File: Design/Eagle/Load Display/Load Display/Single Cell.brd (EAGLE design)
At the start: 68.2 x 83.8 mm, 12 parts

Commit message: Merge remote-tracking branch 'remotes/origin/Panic_Mode_Ben' into HEAD
Conflicts:
	Python/Master.py
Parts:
- removed 12VPOWER, I2C: M025MM, Ben-SF-Con:SCREWTERMINAL-5MM-2
- added JP2: (no value), Ben-SF-Con:2X3-SHROUDED
- added LED2: TLLR4400, led:LED3MM
- added R8: 1000, Ben-rcl:0207/15
- added U$2: (no value), Parts:DRIVER_BOARD_ADAFRUIT
- added U$4, U$5, U$6, U$7: SOLDER_JUMPER, Parts:SOLDER_JUMPER
- added U$8: (no value), Parts:DRIVER_BOARD
- DIS1: device Parts:4INTESTER -> Parts:7SEGMENT_BACKWARDS
- R1, R2, R3, R4, R5: device Ben-rcl:0207/10 -> Ben-rcl:0207/15
- U$1: value 5VREG -> SOLDER_JUMPER; device Parts:LM78XX -> Parts:SOLDER_JUMPER
- U$3: value HT16K33BRD -> SOLDER_JUMPER; device Parts:HT16K33BRKOUT -> Parts:SOLDER_JUMPER
- moved U$1 53.4 mm to (45.7, 26.7), flipped to the bottom, turned to 180 degrees
- moved R2 43.3 mm to (17.8, 69.9)
- moved R3 35.8 mm to (22.9, 11.4)
- moved R1 32.0 mm to (22.9, 69.9)
- moved R6 28.0 mm to (33.0, 69.9)
- moved R7 25.7 mm to (38.1, 69.9)
- moved U$3 24.1 mm to (45.7, 30.5), flipped to the bottom, turned to 180 degrees
- moved DIS1 21.6 mm to (17.8, 1.27)
- moved R4 20.7 mm to (31.7, 11.4)
- moved R5 8.52 mm to (38.1, 11.4)
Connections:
- removed net N$19: U$1.P$3, U$3.VDD
- removed net N$20: 12VPOWER.2, DIS1.8, U$1.P$1
- new net GND: JP2.2, JP2.6, LED2.K, U$1.P$1, U$2.G, U$2.GND, U$4.P$1, U$6.P$1, U$8.G, U$8.GND
- new net N$29: U$1.P$2, U$2.A0, U$3.P$1, U$8.A0
- new net SDA: JP2.3, U$2.SDA, U$8.SDA
- new net SSCL: JP2.4, U$2.SCL, U$8.SCL
- new net VCC12: DIS1.3, DIS1.8, JP2.1
- new net VCC5: JP2.5, R8.1, U$2.VCC, U$3.P$2, U$5.P$2, U$7.P$2, U$8.VCC
- net N$10: now also U$2.DRAIN2, U$8.DRAIN2; no longer U$3.C2
- net N$11: now also U$2.DRAIN3, U$8.DRAIN3; no longer U$3.C3
- net N$12: now also U$2.DRAIN4, U$8.DRAIN4; no longer U$3.C4
- net N$13: now also U$2.DRAIN5, U$8.DRAIN5; no longer U$3.C5
- net N$14: now also U$2.DRAIN6, U$8.DRAIN6; no longer U$3.C6
- net N$15: now also U$2.A1, U$4.P$2, U$5.P$1, U$8.A1; no longer I2C.1, U$3.SDA
- net N$16: now also U$2.A2, U$6.P$2, U$7.P$1, U$8.A2; no longer I2C.2, U$3.SCL
- net N$17: now also U$2.DRAIN7, U$8.DRAIN7; no longer 12VPOWER.1, U$1.P$2, U$3.GND
- net N$18: now also LED2.A, R8.2; no longer DIS1.5, U$3.C7
- net N$8: now also U$2.DRAIN0, U$8.DRAIN0; no longer U$3.C0
- net N$9: now also U$2.DRAIN1, U$8.DRAIN1; no longer U$3.C1
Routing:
- net GND: track 0.00 -> 172.5 mm
- net VCC12: track 0.00 -> 129.1 mm
- net VCC5: track 0.00 -> 93.9 mm
- net SSCL: track 0.00 -> 79.7 mm
- net N$10: track 99.1 -> 44.4 mm
- net N$11: track 72.4 -> 23.7 mm
- net N$16: track 50.8 -> 9.42 mm
- net N$18: track 41.2 -> 3.81 mm
- net N$20: track 35.8 -> 0.00 mm, vias 0 -> 1
- net N$9: track 15.0 -> 43.8 mm
- net N$19: track 26.9 -> 0.00 mm, vias 0 -> 1
- net N$7: track 25.7 -> 2.54 mm
- net N$12: track 48.4 -> 25.9 mm
- net N$17: track 23.4 -> 2.54 mm
- net N$6: track 22.6 -> 2.54 mm
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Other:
- board size 68.2 x 83.8 mm -> 47.9 x 81.3 mm

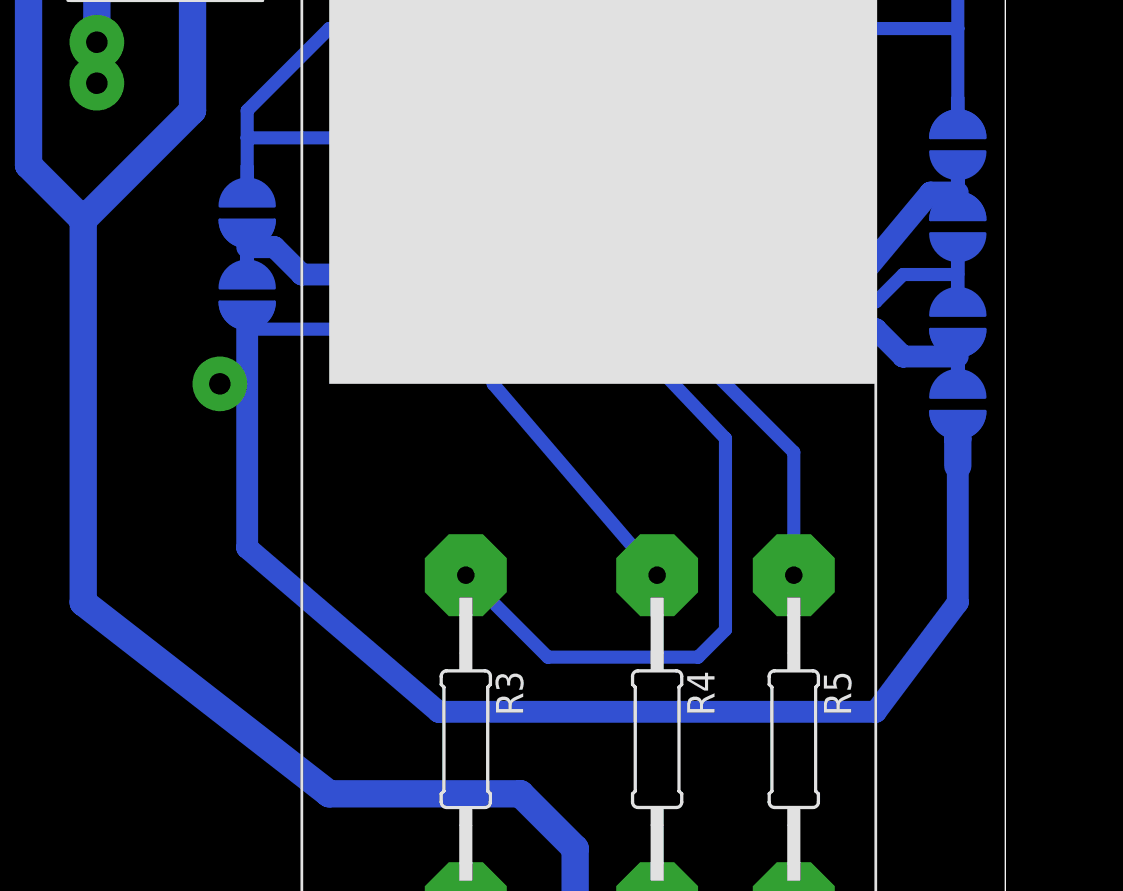
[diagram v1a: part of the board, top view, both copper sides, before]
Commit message: Changed the eagle board to run the 5v in a better path.
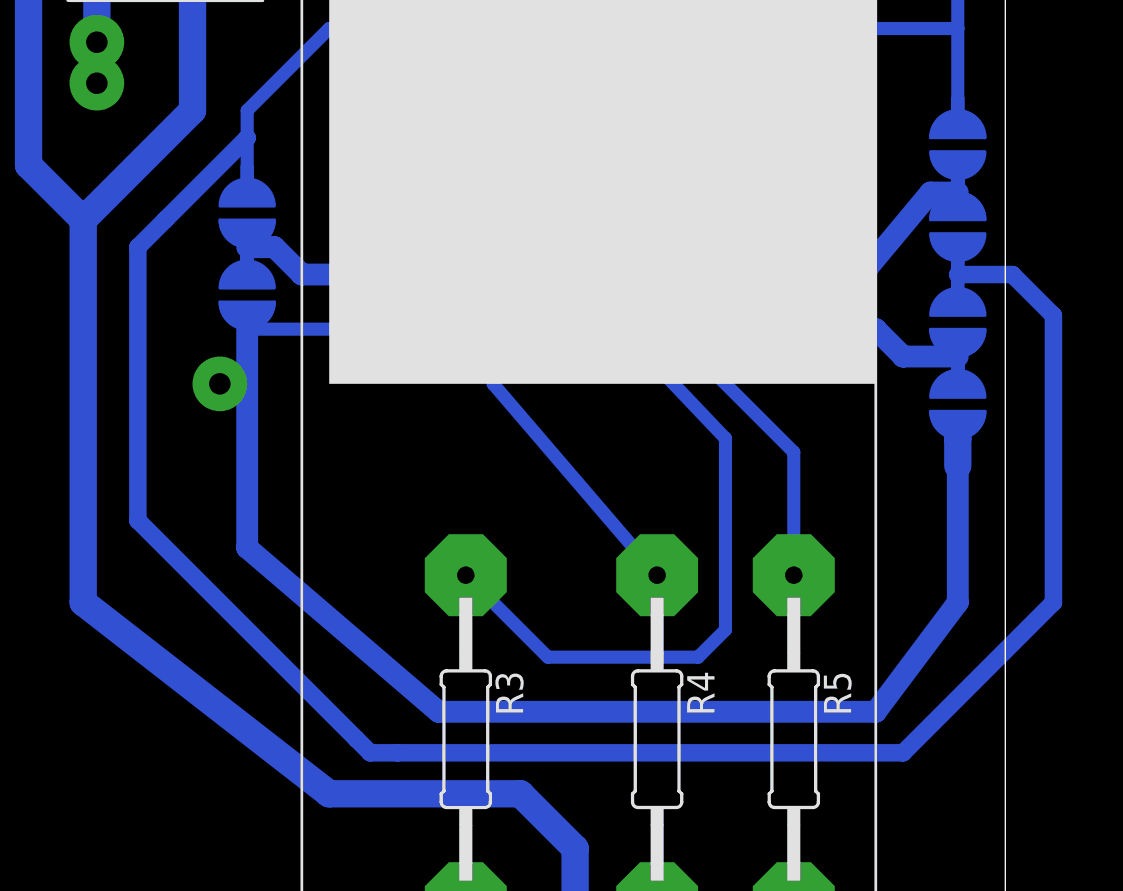
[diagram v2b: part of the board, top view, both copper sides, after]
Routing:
- net VCC5: track 93.9 -> 132.5 mm
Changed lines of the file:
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@@
 <param name="mtCopper" value="0.035mm 0.035mm 0.035mm 0.035mm 0.035mm 0.035mm 0.035mm 0.035mm 0.035mm 0.035mm 0.035mm 0.035mm 0.035mm 0.035mm 0.035mm 0.035mm"/>
 <param name="mtIsolate" value="1.5mm 0.15mm 0.2mm 0.15mm 0.2mm 0.15mm 0.2mm 0.15mm 0.2mm 0.15mm 0.2mm 0.15mm 0.2mm 0.15mm 0.2mm"/>
-<param name="mdWireWire" value="8mil"/>
-<param name="mdWirePad" value="8mil"/>
-<param name="mdWireVia" value="8mil"/>
-<param name="mdPadPad" value="8mil"/>
-<param name="mdPadVia" value="8mil"/>
-<param name="mdViaVia" value="8mil"/>
-<param name="mdSmdPad" value="8mil"/>
-<param name="mdSmdVia" value="8mil"/>
-<param name="mdSmdSmd" value="8mil"/>
+<param name="mdWireWire" value="10mil"/>
+<param name="mdWirePad" value="10mil"/>
+<param name="mdWireVia" value="10mil"/>
+<param name="mdPadPad" value="10mil"/>
+<param name="mdPadVia" value="10mil"/>
+<param name="mdViaVia" value="10mil"/>
+<param name="mdSmdPad" value="10mil"/>
+<param name="mdSmdVia" value="10mil"/>
+<param name="mdSmdSmd" value="10mil"/>
 <param name="mdViaViaSameLayer" value="8mil"/>
 <param name="mnLayersViaInSmd" value="2"/>
@@
 <wire x1="12.70025625" y1="39.3707875" x2="12.70025625" y2="37.4657125" width="0.6096" layer="16"/>
 <wire x1="45.72091875" y1="33.655709375" x2="45.72091875" y2="33.020659375" width="0.6096" layer="16"/>
-<wire x1="45.72091875" y1="33.020659375" x2="43.1808625" y2="33.020659375" width="0.6096" layer="16"/>
-<wire x1="43.1808625" y1="33.020659375" x2="41.9108375" y2="31.750634375" width="0.6096" layer="16"/>
-<wire x1="41.9108375" y1="31.750634375" x2="35.560709375" y2="31.750634375" width="0.6096" layer="16"/>
-<wire x1="35.560709375" y1="31.750634375" x2="35.560709375" y2="34.290684375" width="0.6096" layer="16"/>
-<wire x1="35.560709375" y1="34.290684375" x2="40.6408125" y2="34.290684375" width="0.6096" layer="16"/>
-<wire x1="40.6408125" y1="34.290684375" x2="40.6408125" y2="36.8307375" width="0.6096" layer="16"/>
-<wire x1="40.6408125" y1="36.8307375" x2="33.020659375" y2="36.8307375" width="0.6096" layer="16"/>
-<wire x1="33.020659375" y1="36.8307375" x2="30.480609375" y2="39.3707875" width="0.6096" layer="16"/>
-<wire x1="30.480609375" y1="39.3707875" x2="12.70025625" y2="39.3707875" width="0.6096" layer="16"/>
+<wire x1="12.70025625" y1="39.3707875" x2="12.700253125" y2="39.3707875" width="0.8128" layer="16"/>
+<wire x1="12.700253125" y1="39.3707875" x2="8.890178125" y2="35.5607125" width="0.8128" layer="16"/>
+<wire x1="8.890178125" y1="35.5607125" x2="8.890178125" y2="35.560709375" width="0.8128" layer="16"/>
+<wire x1="8.890178125" y1="35.560709375" x2="7.620153125" y2="34.290684375" width="0.8128" layer="16"/>
+<wire x1="7.620153125" y1="34.290684375" x2="7.620153125" y2="21.59043125" width="0.8128" layer="16"/>
+<wire x1="7.620153125" y1="21.59043125" x2="17.78035625" y2="11.430228125" width="0.8128" layer="16"/>
+<wire x1="17.78035625" y1="11.430228125" x2="18.414771875" y2="10.795228125" width="0.8128" layer="16"/>
+<wire x1="18.414771875" y1="10.795228125" x2="19.685" y2="10.795" width="0.8128" layer="16"/>
+<wire x1="19.685" y1="10.795" x2="43.18" y2="10.795" width="0.8128" layer="16"/>
+<wire x1="43.18" y1="10.795" x2="50.165" y2="17.78" width="0.8128" layer="16"/>
+<wire x1="50.165" y1="17.78" x2="50.165" y2="31.115" width="0.8128" layer="16"/>
+<wire x1="50.165" y1="31.115" x2="48.26" y2="33.02" width="0.8128" layer="16"/>
+<wire x1="48.26" y1="33.02" x2="45.721578125" y2="33.02" width="0.8128" layer="16"/>
+<wire x1="45.721578125" y1="33.02" x2="45.72091875" y2="33.020659375" width="0.8128" layer="16"/>
 <wire x1="45.72091875" y1="33.020659375" x2="45.720915625" y2="32.385609375" width="0" layer="19" extent="16-16"/>
 </signal>
@@
 </signal>
 </signals>
-<errors>
-</errors>
 </board>
 </drawing>
